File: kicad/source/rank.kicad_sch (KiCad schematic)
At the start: 18 parts, among them IC8 SN74HC148NSR

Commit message: completed PCB fab setup
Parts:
- S2, S3, S4, S5, S6, S7, S8, S9: now not fitted
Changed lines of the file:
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@@
 		(in_bom yes)
 		(on_board yes)
-		(dnp no)
+		(dnp yes)
 		(fields_autoplaced yes)
 		(property "Reference" "S4"
@@
 		(in_bom yes)
 		(on_board yes)
-		(dnp no)
+		(dnp yes)
 		(fields_autoplaced yes)
 		(property "Reference" "S9"
@@
 		(in_bom yes)
 		(on_board yes)
-		(dnp no)
+		(dnp yes)
 		(fields_autoplaced yes)
 		(property "Reference" "S6"
@@
 		(in_bom yes)
 		(on_board yes)
-		(dnp no)
+		(dnp yes)
 		(fields_autoplaced yes)
 		(property "Reference" "S3"
@@
 		(in_bom yes)
 		(on_board yes)
-		(dnp no)
+		(dnp yes)
 		(fields_autoplaced yes)
 		(property "Reference" "S8"
@@
 		(in_bom yes)
 		(on_board yes)
-		(dnp no)
+		(dnp yes)
 		(fields_autoplaced yes)
 		(property "Reference" "S5"
@@
 		(in_bom yes)
 		(on_board yes)
-		(dnp no)
+		(dnp yes)
 		(fields_autoplaced yes)
 		(property "Reference" "S7"
@@
 		(in_bom yes)
 		(on_board yes)
-		(dnp no)
+		(dnp yes)
 		(fields_autoplaced yes)
 		(property "Reference" "S2"

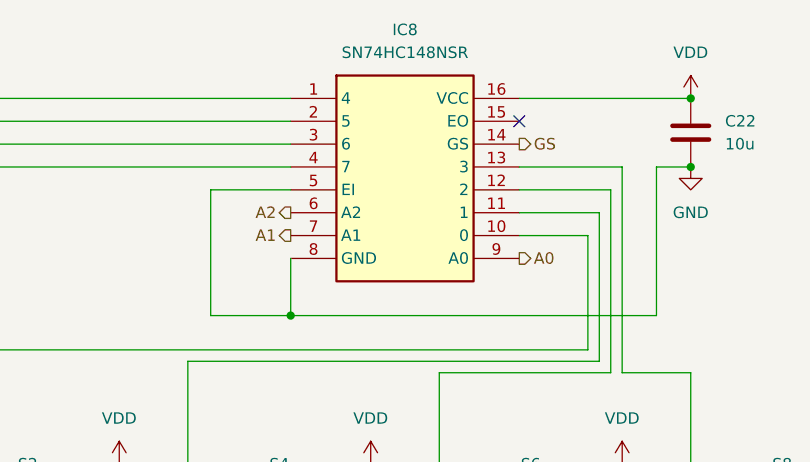
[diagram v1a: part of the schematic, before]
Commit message: adjusted PCB fab setup for faster manufacturing
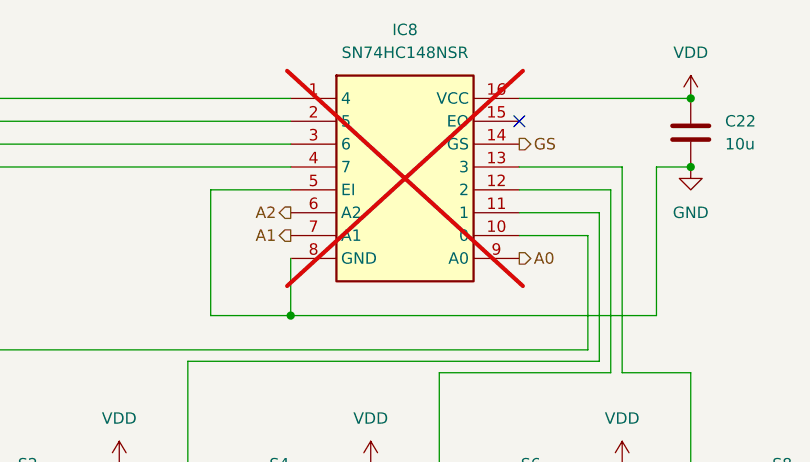
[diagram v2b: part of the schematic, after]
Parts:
- IC8: now not fitted
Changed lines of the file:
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@@
 		(in_bom yes)
 		(on_board yes)
-		(dnp no)
+		(dnp yes)
 		(fields_autoplaced yes)
 		(property "Reference" "IC8"
